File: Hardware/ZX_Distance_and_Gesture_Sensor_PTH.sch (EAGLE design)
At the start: 49 parts, among them Q1 MMBT2222A, Q2 MOSFET-NCHANNEL2N7002PW, U1 PIC16F1823-14PINTSSOP, U2 MCP6021T-E/OT, U3 DMC2700UDM, U4 DMC2700UDM, U5 BRM-2A18VERT, U6 TSOP57238TT1

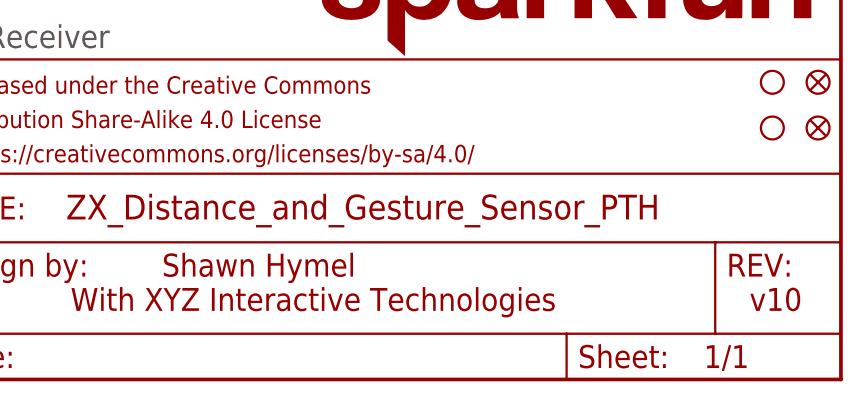
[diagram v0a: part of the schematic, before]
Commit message: Updated GestureSense Logo
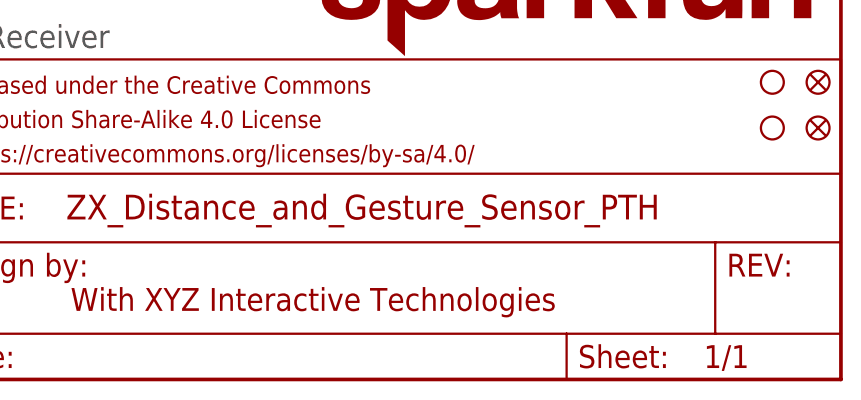
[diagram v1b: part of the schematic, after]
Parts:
- FRAME1: value (none) -> FRAME-LETTER; DESIGNER Shawn Hymel -> (none); VERSION v10 -> (none)
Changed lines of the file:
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@@
 </classes>
 <parts>
-<part name="FRAME1" library="SparkFun-Aesthetics" deviceset="FRAME-LETTER" device="">
-<attribute name="DESIGNER" value="Shawn Hymel"/>
-<attribute name="VERSION" value="v10"/>
-</part>
+<part name="FRAME1" library="SparkFun-Aesthetics" deviceset="FRAME-LETTER" device=""/>
 <part name="U1" library="SparkFun-DigitalIC" deviceset="PIC16F1823-14PIN" device="TSSOP"/>
 <part name="U2" library="SparkFun-AnalogIC" deviceset="MCP6021" device="T-E/OT"/>
@@
 </plain>
 <instances>
-<instance part="FRAME1" gate="G$1" x="0" y="0" smashed="yes">
-<attribute name="DESIGNER" x="173.482" y="11.43" size="2.54" layer="94"/>
-<attribute name="VERSION" x="238.76" y="7.62" size="2.54" layer="94"/>
-</instance>
+<instance part="FRAME1" gate="G$1" x="0" y="0" smashed="yes"/>
 <instance part="FRAME1" gate="V" x="147.32" y="0"/>
 <instance part="U1" gate="G$1" x="203.2" y="165.1" smashed="yes">
